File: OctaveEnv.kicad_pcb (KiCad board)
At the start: 4 copper layers, 100 x 65 mm, 89 parts, among them J101 IN, J102 PWR, J103 OUT, Q101 BC857, SW101 Stomp, U101 AZ34063U, U102 L7805, U103 TL074, U104 74HCT74, U105 LM13700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

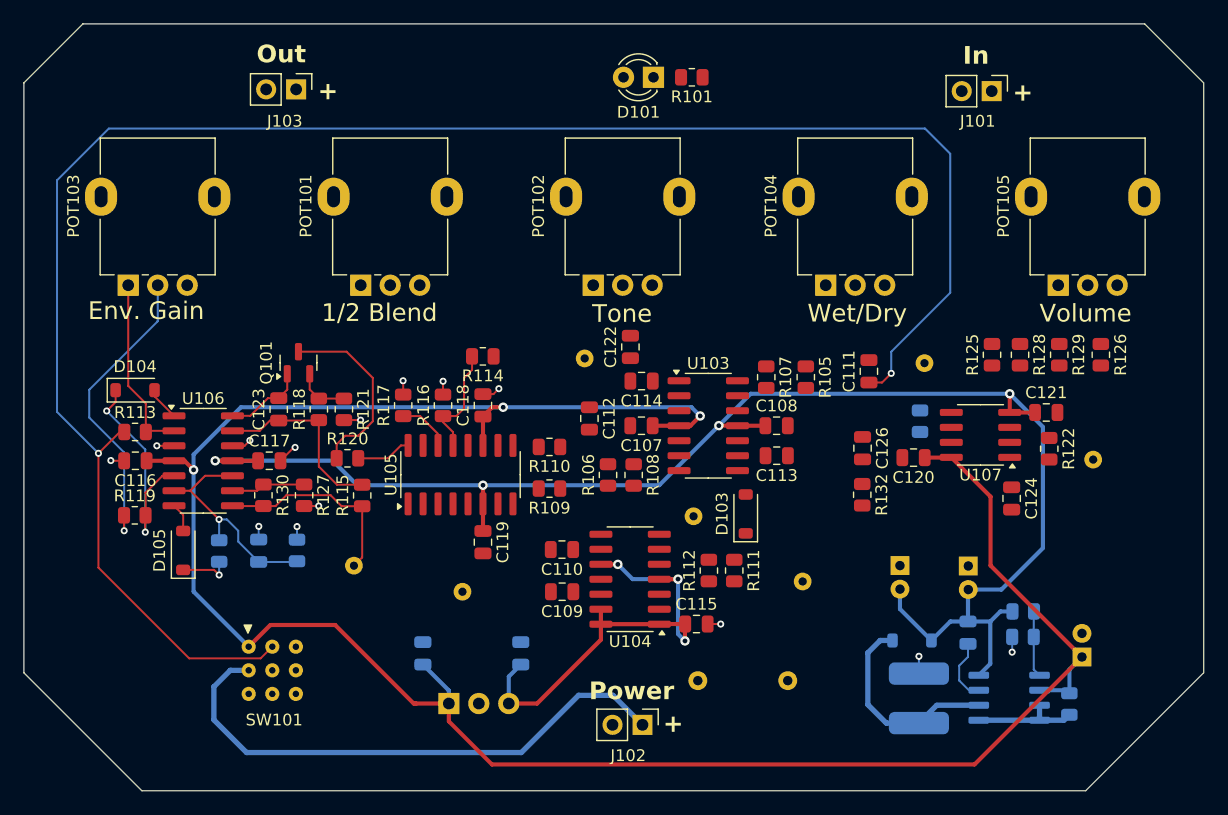
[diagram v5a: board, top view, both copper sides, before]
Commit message: routing done, DRC passing
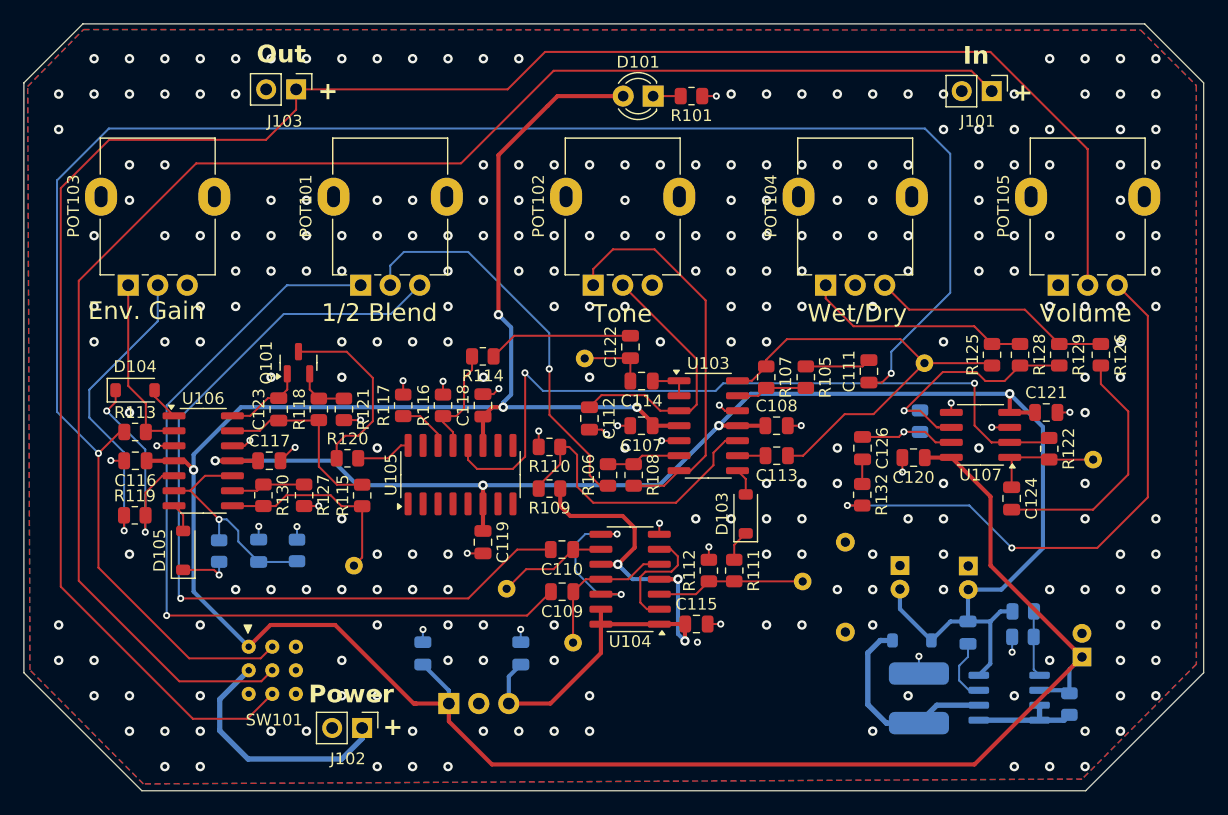
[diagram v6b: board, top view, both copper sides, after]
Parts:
- moved J102 23.8 mm to (28.7, 59.7)
- moved TP106 14.8 mm to (46.5, 52.5), turned to 180 degrees
- moved R133 13.2 mm to (69.6, 51.5), turned to 90 degrees
- moved TP107 3.75 mm to (40.9, 47.9)
- moved D101 1.59 mm to (53.3, 6.12)
- moved R101 1.59 mm to (56.6, 6.12)
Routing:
- net JACK_OUT: track 0.00 -> 165.0 mm
- net JACK_IN: track 0.00 -> 131.2 mm
- net Net-(C110-Pad2): track 0.00 -> 73.5 mm, vias 0 -> 1
- net Net-(C109-Pad2): track 0.00 -> 71.9 mm, vias 0 -> 1
- net Net-(U107A--): track 0.00 -> 63.6 mm, vias 0 -> 2
- net Net-(POT105-Pad3): track 0.00 -> 49.1 mm, vias 0 -> 2
- net GTR_GAIN: track 0.00 -> 39.1 mm
- net Net-(POT101-Pad2): track 0.00 -> 33.9 mm, vias 0 -> 1
- net Net-(POT102-Pad1): track 0.00 -> 33.7 mm
- net +9V: track 191.4 -> 220.4 mm, vias 3 -> 4
- net Net-(J102-Pin_1): track 46.9 -> 20.8 mm
- net Net-(U103C-+): track 0.00 -> 25.7 mm
- net Net-(U103A-+): track 0.00 -> 23.0 mm
- net Net-(C124-Pad2): track 0.00 -> 21.3 mm
- net Net-(U107B--): track 0.00 -> 21.3 mm, vias 0 -> 1
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- added copper zone on B.Cu, net GND
- added copper zone on F.Cu, net GND

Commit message: rev1 gerbers ready
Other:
- board text added: "Octave Mod"
- board text added: "Rev. 1 Dec 2024 Hayden Setlik"

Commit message: rev1 sent to fab
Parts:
- added TP108: SWC, TestPoint:TestPoint_THTPad_D1.5mm_Drill0.7mm_VAL, B.Cu at (92.5, 58.5)
- added TP109: SWE, TestPoint:TestPoint_THTPad_D1.5mm_Drill0.7mm_VAL, B.Cu at (69.9, 55.6)
- moved SW101 3.60 mm to (17.6, 59.8)
- moved J102 1.56 mm to (28.3, 58.2)
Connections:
- net Net-(D102-K) renamed /SWE
- net Net-(U101-DRC) renamed /SWC
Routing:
- net /SWC: track 9.14 -> 13.1 mm
- net JACK_OUT: track 165.0 -> 161.1 mm
- net +9V: track 220.4 -> 223.9 mm
- net JACK_IN: track 131.2 -> 128.1 mm
- net FX_IN: track 156.9 -> 153.8 mm
- net Net-(J102-Pin_1): track 20.8 -> 23.3 mm
- net /SWE: track 17.6 -> 19.2 mm
- net GND: vias 277 -> 30
